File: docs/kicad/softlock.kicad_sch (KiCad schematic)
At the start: 1 part

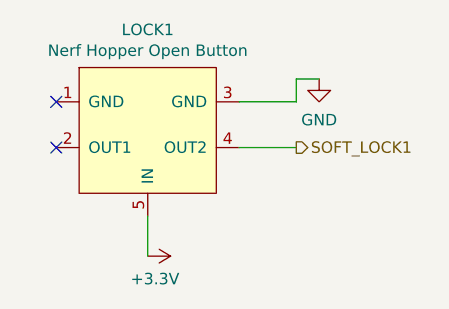
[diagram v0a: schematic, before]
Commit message: Updating PCB to match schematic.
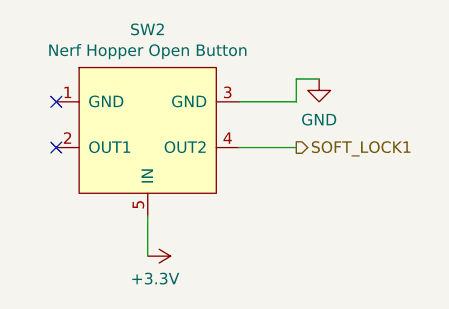
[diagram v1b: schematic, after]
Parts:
- renumbered LOCK1 to SW2
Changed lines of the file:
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@@
   (symbol (lib_id "Nemesis-Mod:Nerf_Hopper_Lock") (at 143.51 100.33 0) (unit 1)
     (in_bom yes) (on_board yes)
-    (property "Reference" "LOCK1" (id 0) (at 143.51 89.789 0))
+    (property "Reference" "SW2" (id 0) (at 143.51 89.789 0))
     (property "Value" "Nerf Hopper Open Button" (id 1) (at 143.51 92.1004 0))
     (property "Footprint" "" (id 2) (at 143.51 92.71 0)
